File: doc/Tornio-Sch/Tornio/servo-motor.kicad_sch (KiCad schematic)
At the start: 0 parts

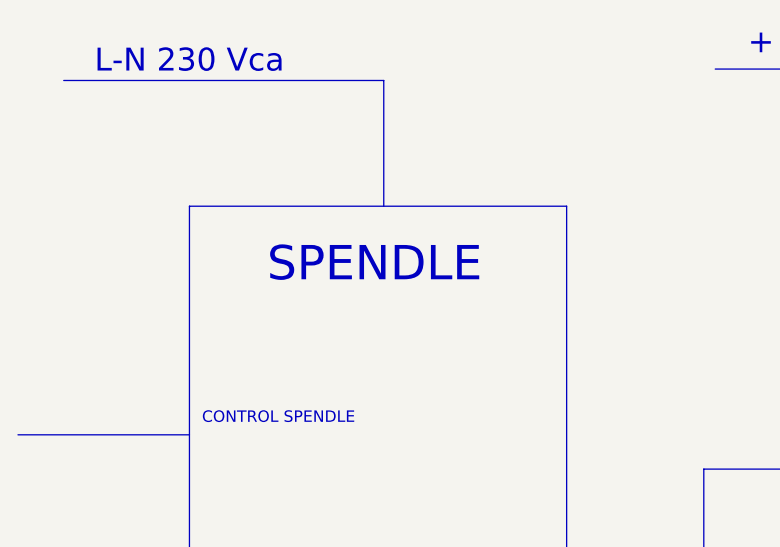
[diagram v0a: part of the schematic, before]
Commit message: spindle protection
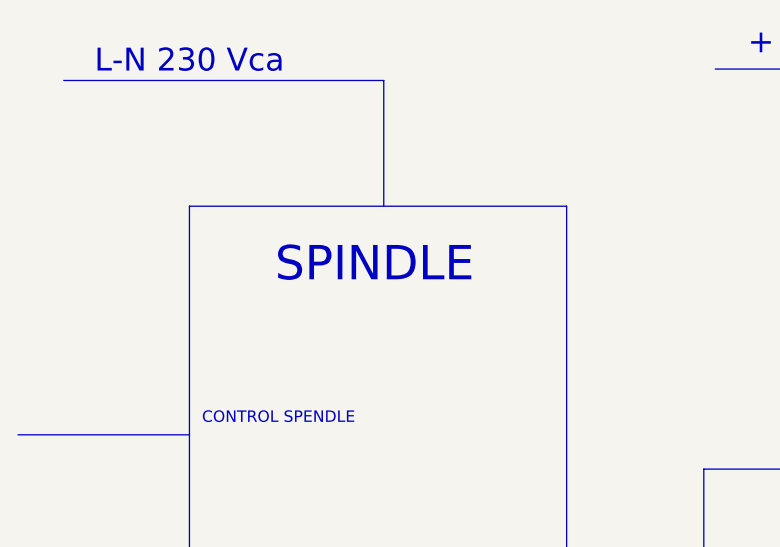
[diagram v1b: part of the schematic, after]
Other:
- note added: "SPINDLE"
- note removed: "SPENDLE"
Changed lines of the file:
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@@
 (kicad_sch
-	(version 20240812)
+	(version 20250114)
 	(generator "eeschema")
-	(generator_version "8.99")
+	(generator_version "9.0")
 	(paper "A4")
 	(rectangle
@@
 		)
 	)
-	(text "SPENDLE"
+	(text "SPINDLE"
 		(exclude_from_sim no)
 		(at 77.724 48.514 0)
